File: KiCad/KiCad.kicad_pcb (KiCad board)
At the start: 2 copper layers, 96.1 x 96.7 mm, 91 parts, among them J1 SSK02-FPH-254-A2, J10 footswitch3, J14 powerRailAndBatteryGround, J16 Barrel3andbarrel2, J17 Guitar input, J18 positivePowerInputs, J19 positivePowerInputs, J2 SSK02-FPH-254-A3, J3 SSK02-FPH-254-A3, J4 SSK02-FPH-254-A3, J5 footswitch1, J6 footswitch2, J7 SSK02-FPH-254-A2, J8 SSK02-FPH-254-A2, J9 SSK02-FPH-254-A3, U1 LT1054, U10 PCM5102APW, U13 MCP1703T-5002E/DB, U14 MCP1703T-5002E/DB, U15 MCP1703T-3302E/DB, U2 PMEG2005CT_215, U5 PCM1808-Q1_PW_14, U6 NE5532, U7 NE5532

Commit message: Changes Luke caught
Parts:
- removed TP4: TestPoint, TestPoint:TestPoint_Loop_D2.50mm_Drill1.85mm
- added REF**: MountingHole_3.2mm_M3_ISO14580_Pad_TopBottom, MountingHole:MountingHole_3.2mm_M3_ISO14580_Pad_TopBottom, F.Cu at (169.3, 62.1)
- added REF**: MountingHole_3.2mm_M3_ISO14580_Pad_TopBottom, MountingHole:MountingHole_3.2mm_M3_ISO14580_Pad_TopBottom, F.Cu at (257.3, 149.9)
- added REF**: MountingHole_3.2mm_M3_ISO14580_Pad_TopBottom, MountingHole:MountingHole_3.2mm_M3_ISO14580_Pad_TopBottom, F.Cu at (169.3, 149.9)
- added REF**: MountingHole_3.2mm_M3_ISO14580_Pad_TopBottom, MountingHole:MountingHole_3.2mm_M3_ISO14580_Pad_TopBottom, F.Cu at (257.3, 62.1)
- U13, U14: footprint lin_reg_50:SOT-223_3MC_MCH -> lin_reg50:SOT-223_3MC_MCH
- U15: footprint lin_reg:SOT-223_3MC_MCH -> lin_reg33:SOT-223_3MC_MCH
- moved R10 2.76 mm to (223.1, 62.0), turned to 90 degrees
- moved R9 2.66 mm to (220.3, 62.0), turned to -90 degrees
- moved C24 0.51 mm to (226.4, 147.8)
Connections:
- R10 pad 1: GND -> Net-(U7A-+)
- R10 pad 2: Net-(U7A-+) -> +9V
- R9 pad 1: Net-(U7A-+) -> GND
- R9 pad 2: +9V -> Net-(U7A-+)
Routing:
- net GND: track 123.0 -> 138.6 mm, vias 52 -> 53
- net +3.3VA: track 49.2 -> 57.8 mm, vias 0 -> 2
- net Net-(R4-Pad2): track 13.5 -> 9.21 mm
- net -9V: track 184.9 -> 187.4 mm
- net +5VA: track 123.6 -> 122.0 mm
- net Net-(U10-OUTL): track 8.66 -> 9.63 mm
- net +9V: track 230.0 -> 230.7 mm
- net +5VD: track 85.4 -> 84.7 mm

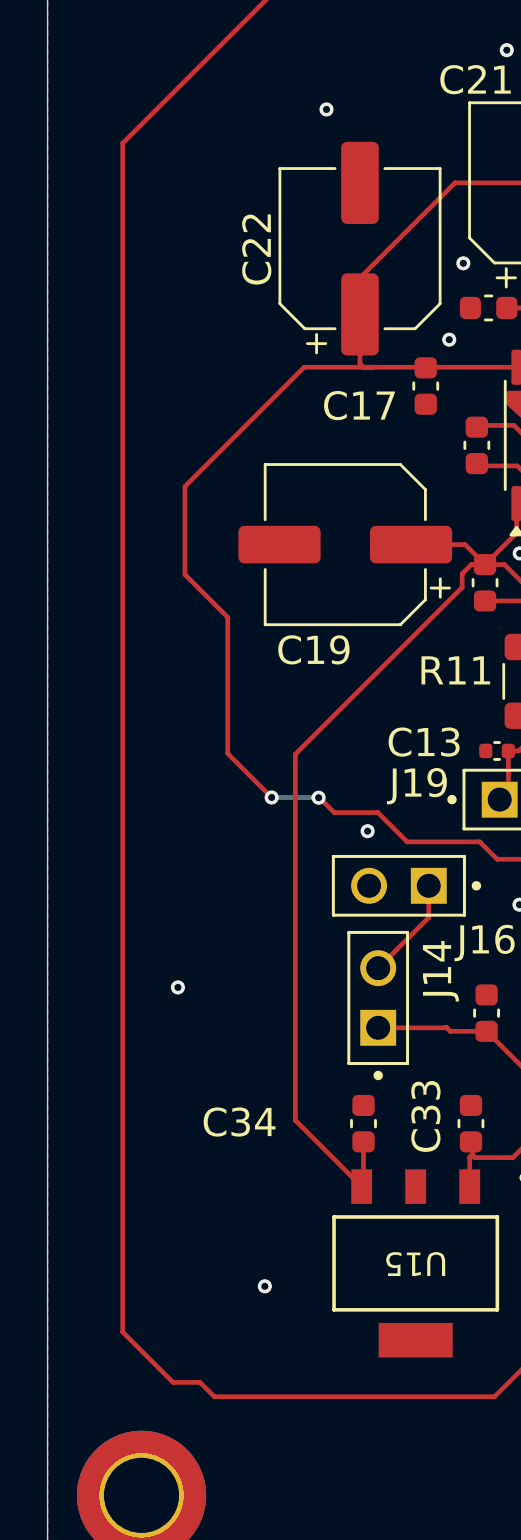
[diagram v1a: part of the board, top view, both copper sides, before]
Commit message: Changes to the BoM
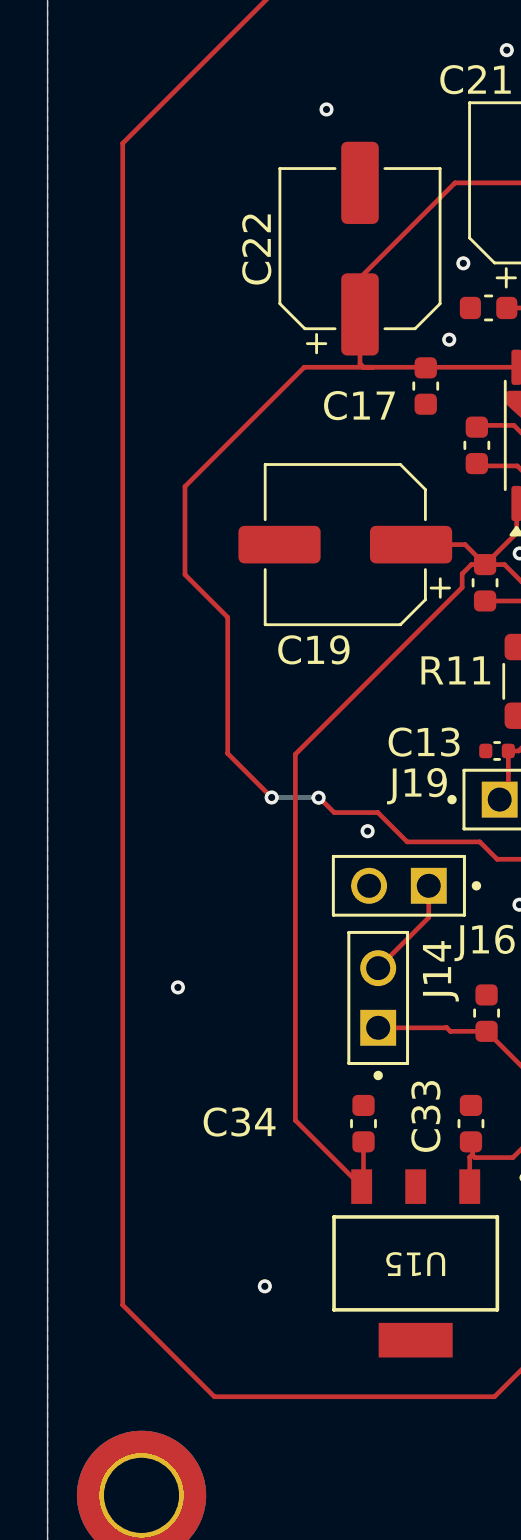
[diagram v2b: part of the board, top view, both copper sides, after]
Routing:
- net +5VA: track 122.0 -> 121.3 mm
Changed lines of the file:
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@@
+	)
+	(segment
+		(start 196.37 79.49)
+		(end 198.575 81.695)
+		(width 0.2)
+		(layer "F.Cu")
+		(net "+5VA")
 	)
 	(segment
 		(start 198.575 82.925)
 		(end 198.575 83.185)
+		(width 0.2)
+		(layer "F.Cu")
+		(net "+5VA")
+	)
+	(segment
+		(start 188.25 134.8)
+		(end 188.25 136.731)
+		(width 0.2)
+		(layer "F.Cu")
+		(net "+5VA")
+	)
+	(segment
+		(start 168.55 141.8)
+		(end 168.55 92.34)
+		(width 0.2)
+		(layer "F.Cu")
+		(net "+5VA")
+	)
+	(segment
+		(start 181.4 79.49)
+		(end 196.37 79.49)
+		(width 0.2)
+		(layer "F.Cu")
+		(net "+5VA")
+	)
+	(segment
+		(start 198.575 83.185)
+		(end 200.355001 84.965001)
+		(width 0.2)
+		(layer "F.Cu")
+		(net "+5VA")
+	)
+	(segment
+		(start 188.225 136.756)
+		(end 187.004 136.756)
+		(width 0.2)
+		(layer "F.Cu")
+		(net "+5VA")
+	)
+	(segment
+		(start 200.355001 84.965001)
+		(end 201.2717 84.965001)
+		(width 0.2)
+		(layer "F.Cu")
+		(net "+5VA")
+	)
+	(segment
+		(start 172.45 145.7)
+		(end 168.55 141.8)
+		(width 0.2)
+		(layer "F.Cu")
+		(net "+5VA")
+	)
+	(segment
+		(start 187.004 136.756)
+		(end 185.63 138.13)
+		(width 0.2)
+		(layer "F.Cu")
+		(net "+5VA")
+	)
+	(segment
+		(start 198.575 81.695)
+		(end 198.575 82.925)
+		(width 0.2)
+		(layer "F.Cu")
+		(net "+5VA")
+	)
+	(segment
+		(start 185.63 144.45)
+		(end 184.38 145.7)
+		(width 0.2)
+		(layer "F.Cu")
+		(net "+5VA")
+	)
+	(segment
+		(start 185.63 138.13)
+		(end 185.63 144.45)
+		(width 0.2)
+		(layer "F.Cu")
+		(net "+5VA")
+	)
+	(segment
+		(start 168.55 92.34)
+		(end 181.4 79.49)
 		(width 0.2)
 		(layer "F.Cu")
@@
 	)
 	(segment
-		(start 188.25 134.8)
-		(end 188.25 136.731)
-		(width 0.2)
-		(layer "F.Cu")
-		(net "+5VA")
-	)
-	(segment
-		(start 185.63 144.45)
-		(end 184.38 145.7)
-		(width 0.2)
-		(layer "F.Cu")
-		(net "+5VA")
-	)
-	(segment
-		(start 172.45 145.7)
-		(end 171.84 145.09)
-		(width 0.2)
-		(layer "F.Cu")
-		(net "+5VA")
-	)
-	(segment
-		(start 188.225 136.756)
-		(end 187.004 136.756)
-		(width 0.2)
-		(layer "F.Cu")
-		(net "+5VA")
-	)
-	(segment
-		(start 198.575 83.185)
-		(end 200.355001 84.965001)
-		(width 0.2)
-		(layer "F.Cu")
-		(net "+5VA")
-	)
-	(segment
-		(start 200.355001 84.965001)
-		(end 201.2717 84.965001)
-		(width 0.2)
-		(layer "F.Cu")
-		(net "+5VA")
-	)
-	(segment
-		(start 168.55 142.95)
-		(end 168.55 92.34)
-		(width 0.2)
-		(layer "F.Cu")
-		(net "+5VA")
-	)
-	(segment
-		(start 171.84 145.09)
-		(end 170.69 145.09)
-		(width 0.2)
-		(layer "F.Cu")
-		(net "+5VA")
-	)
-	(segment
-		(start 198.575 81.695)
-		(end 198.575 82.925)
-		(width 0.2)
-		(layer "F.Cu")
-		(net "+5VA")
-	)
-	(segment
-		(start 181.4 79.49)
-		(end 196.37 79.49)
-		(width 0.2)
-		(layer "F.Cu")
-		(net "+5VA")
-	)
-	(segment
-		(start 185.63 138.13)
-		(end 185.63 144.45)
-		(width 0.2)
-		(layer "F.Cu")
-		(net "+5VA")
-	)
-	(segment
 		(start 188.25 136.731)
 		(end 188.225 136.756)
 		(width 0.2)
 		(layer "F.Cu")
-		(net "+5VA")
-	)
-	(segment
-		(start 196.37 79.49)
-		(end 198.575 81.695)
-		(width 0.2)
-		(layer "F.Cu")
-		(net "+5VA")
-	)
-	(segment
-		(start 168.55 92.34)
-		(end 181.4 79.49)
-		(width 0.2)
-		(layer "F.Cu")
-		(net "+5VA")
-	)
-	(segment
-		(start 187.004 136.756)
-		(end 185.63 138.13)
-		(width 0.2)
-		(layer "F.Cu")
-		(net "+5VA")
-	)
-	(segment
-		(start 170.69 145.09)
-		(end 168.55 142.95)
-		(width 0.2)
-		(layer "F.Cu")

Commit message: done
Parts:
- added G***: Guitar_Rocker_Art_40mm, dr_li:Guitar_Rocker_Art_40mm, B.Cu at (103.2, 139.0)
- U1: value LT1054 -> LT1054CDWR; footprint charge_pump:SOIC127P1030X265-16N -> lt1054_16soic:DW16-M
- moved C24 16.3 mm to (212.3, 139.6), turned to -90 degrees
- moved C25 4.13 mm to (236.2, 140.6)
- moved U1 1.04 mm to (223.5, 137.8), turned to 0 degrees
- moved U13 0.08 mm to (200.0, 139.9)
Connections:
- A1 pad 13: unconnected-(A1-GND-Pad13)_3 -> GND
- A1 pad 18: unconnected-(A1-GND-Pad13)_5 -> GND
- A1 pad 23: unconnected-(A1-GND-Pad13)_13 -> GND
- A1 pad 28: unconnected-(A1-GND-Pad13)_4 -> GND
- A1 pad 3: unconnected-(A1-GND-Pad13)_6 -> GND
- A1 pad 33: unconnected-(A1-AGND-Pad33) -> GND
- A1 pad 38: unconnected-(A1-GND-Pad13)_10 -> GND
- A1 pad 8: unconnected-(A1-GND-Pad13)_12 -> GND
- U1 pad 10: (no net) -> unconnected-(U1-NC-Pad10)
- U1 pad 11: (no net) -> -9V
- U1 pad 12: (no net) -> unconnected-(U1-VREF-Pad12)
- U1 pad 13: (no net) -> unconnected-(U1-OSC-Pad13)
- U1 pad 14: (no net) -> +9V
- U1 pad 15: (no net) -> unconnected-(U1-NC-Pad15)
- U1 pad 16: (no net) -> unconnected-(U1-NC-Pad16)
- U1 pad 2: Net-(U1-CAP+) -> unconnected-(U1-NC-Pad2)
- U1 pad 3: GND -> unconnected-(U1-FB/SD-Pad3)
- U1 pad 4: Net-(U1-CAP-) -> Net-(U1-CAP+)
- U1 pad 5: -9V -> GND
- U1 pad 6: unconnected-(U1-VREF-Pad6) -> Net-(U1-CAP-)
- U1 pad 8: +9V -> unconnected-(U1-NC-Pad8)
- U1 pad 9: (no net) -> unconnected-(U1-NC-Pad9)
- U10 pad 17: GND -> +3.3VA
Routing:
- net +3.3VA: track 57.8 -> 72.5 mm, vias 2 -> 4
- net Net-(U1-CAP-): track 14.1 -> 8.77 mm
- net Net-(U1-CAP+): track 10.9 -> 6.52 mm
- net GND: track 138.6 -> 134.3 mm, vias 53 -> 55
- net +9V: track 230.7 -> 229.4 mm
- net -9V: track 187.4 -> 188.6 mm
